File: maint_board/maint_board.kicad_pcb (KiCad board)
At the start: 2 copper layers, 175.4 x 134.9 mm, 108 parts, among them J1 USB_mini_micro_B, J2 4P4C, J3 TC2030-IDC_FB, K1 KEYSW, K10 KEYSW, K11 KEYSW, K12 KEYSW, K13 KEYSW, K14 KEYSW, K15 KEYSW, K16 KEYSW, K17 KEYSW, K18 KEYSW, K19 KEYSW, K2 KEYSW, K20 KEYSW, K21 KEYSW, K22 KEYSW, K23 KEYSW, K24 KEYSW, K25 KEYSW, K26 KEYSW, K27 KEYSW, K28 KEYSW, K29 KEYSW, K3 KEYSW, K30 KEYSW, K31 KEYSW, K32 KEYSW, K4 KEYSW, K5 KEYSW, K6 KEYSW, K7 KEYSW, K8 KEYSW, K9 KEYSW, SW1 SW_PUSH, U1 ATMEGA32U4, X1 XTAL_GND

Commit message: added libs and worked on layout
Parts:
- removed D14, D21, D22, D23, D24, D25, D26, D27, D28, D32, D7: D, keyboard_parts:D_SOD123_axial
- removed K14, K21, K22, K23, K24, K25, K26, K27, K28, K32, K7: KEYSW, keyswitches:SW_MX_reversible
- moved D31 47.3 mm to (185.7, 97.0)
- moved K31 47.3 mm to (186.2, 92.8)
- moved D30 35.3 mm to (168.6, 114.4)
- moved K30 35.3 mm to (169.5, 110.3)
- moved D29 34.3 mm to (152.5, 111.2)
- moved K29 34.3 mm to (153.1, 107.2)
- moved C13 24.5 mm to (120.5, 105.4)
- moved C15 24.5 mm to (112.4, 105.4)
- moved C10 24.5 mm to (136.5, 105.4)
- moved C11 24.5 mm to (128.5, 105.4)
- moved C12 24.5 mm to (128.5, 105.4)
- moved C14 24.5 mm to (120.5, 105.4)
- moved C16 24.5 mm to (112.4, 105.4)
- moved C9 24.5 mm to (136.5, 105.4)
- moved D33 24.5 mm to (136.5, 101.4)
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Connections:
- D29 pad 1: /keys/Row5 -> /keys/Row4
- D30 pad 1: /keys/Row5 -> /keys/Row4
- D31 pad 1: /keys/Row5 -> /keys/Row4
- U1 pad 36: /keys/Col7 -> (no net)
- U1 pad 37: /keys/Row5 -> (no net)
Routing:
- net /keys/Row4: track 238.1 -> 82.6 mm, vias 4 -> 1
- net /keys/Row5: track 138.1 -> 0.00 mm, vias 1 -> 0
- net VCC: track 209.5 -> 75.8 mm, vias 7 -> 5
- net /keys/Col7: track 108.1 -> 0.00 mm, vias 2 -> 0
- net /Leds/Din: track 7.68 -> 111.1 mm
- net /keys/Col6: track 206.1 -> 117.1 mm, vias 3 -> 1
- net /keys/Col5: track 235.3 -> 156.5 mm
- net /keys/Col4: track 240.2 -> 185.4 mm
- net /keys/Col2: track 227.0 -> 178.8 mm
- net /keys/Row3: track 217.0 -> 168.9 mm, vias 5 -> 2
- net /keys/Col3: track 204.4 -> 156.8 mm
- net /keys/Row2: track 207.5 -> 174.2 mm, vias 5 -> 4
- net /keys/Col1: track 261.3 -> 234.8 mm
- net GND: track 101.3 -> 80.8 mm, vias 24 -> 18
- net /keys/Row1: track 197.8 -> 182.4 mm, vias 2 -> 3
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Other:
- board outline removed

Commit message: Finiched!
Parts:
- added D7: LED, Diode_SMD:D_0603_1608Metric, F.Cu at (170.3, 31.1)
- added Q1: Q_NMOS_GSD, Package_TO_SOT_SMD:SOT-23, F.Cu at (166.9, 32.0)
- added R10: 10k, Resistor_SMD:R_0603_1608Metric, F.Cu at (163.5, 33.0)
- added R9: 500, Resistor_SMD:R_0603_1608Metric, F.Cu at (173.4, 31.1)
- J1: footprint keyboard_parts:USB_miniB_hirose_5S8 -> my_connectors:usb_minib_wm5462ct-nd
- J3: footprint my_connectors:TC2030-IDC-FP -> Connector:Tag-Connect_TC2030-IDC-NL_2x03_P1.27mm_Vertical
- R1, SW1: moved to F.Cu
- moved SW1 30.0 mm to (162.4, 36.9), turned to 0 degrees
- moved R1 28.5 mm to (166.5, 36.9), turned to 180 degrees
- moved D44 21.5 mm to (181.4, 38.4)
- moved D43 19.0 mm to (178.5, 38.4)
- moved C5 18.6 mm to (200.9, 62.8), turned to 270 degrees
- moved C7 17.9 mm to (187.8, 57.2), turned to 180 degrees
- moved J1 17.3 mm to (180.6, 30.6), turned to 270 degrees
- moved D30 14.0 mm to (182.6, 113.7), turned to 350 degrees
- moved K30 13.7 mm to (183.2, 108.9)
- moved D29 12.6 mm to (165.1, 110.4), turned to 350 degrees
- moved K29 12.5 mm to (165.6, 105.9)
- moved J3 5.58 mm to (181.0, 52.0), turned to 90 degrees
- moved R4 5.43 mm to (192.7, 45.7)
- moved R5 4.84 mm to (197.8, 45.6)
- moved J2 3.83 mm to (196.1, 35.0)
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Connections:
- U1 pad 37: (no net) -> Net-(Q1-Pad1)
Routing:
- net VCC: track 75.8 -> 279.0 mm, vias 5 -> 22
- net Net-(Q1-Pad1): track 0.00 -> 64.2 mm, vias 0 -> 3
- net Net-(R1-Pad2): track 0.00 -> 42.2 mm, vias 0 -> 1
- net /mcu/usb_D-: track 5.20 -> 36.7 mm
- net /mcu/usb_D+: track 5.80 -> 34.5 mm
- net GND: track 80.8 -> 106.6 mm, vias 18 -> 30
- net /keys/Col1: track 234.8 -> 210.2 mm, vias 2 -> 1
- net rst_prog: track 0.00 -> 18.9 mm
- net sck_prog: track 0.00 -> 17.3 mm
- net /keys/Col5: track 156.5 -> 172.6 mm, vias 2 -> 3
- net /keys/Col4: track 185.4 -> 201.0 mm
- net mosi_prog: track 0.00 -> 14.4 mm
- net miso_prog: track 0.00 -> 14.0 mm
- net /keys/Row2: track 174.2 -> 160.9 mm, vias 4 -> 0
- net /mcu/SCL: track 29.5 -> 42.6 mm, vias 2 -> 3
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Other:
- board outline added: 151.1 x 90.3 mm
- net class Default: clearance 0.3 -> 0.25
- net class Min added: clearance 0.1, trace_width 0.1, via_dia 0.45, via_drill 0.2
- rule pad_to_mask_clearance: 0.051 -> 0
- rule solder_mask_min_width: 0.25 -> 0.1
- rule trace_clearance: 0.3 -> 0.25
- rule trace_min: 0.2 -> 0.1
- rule via_min_drill: 0.3 -> 0.2
- rule via_min_size: 0.4 -> 0.45

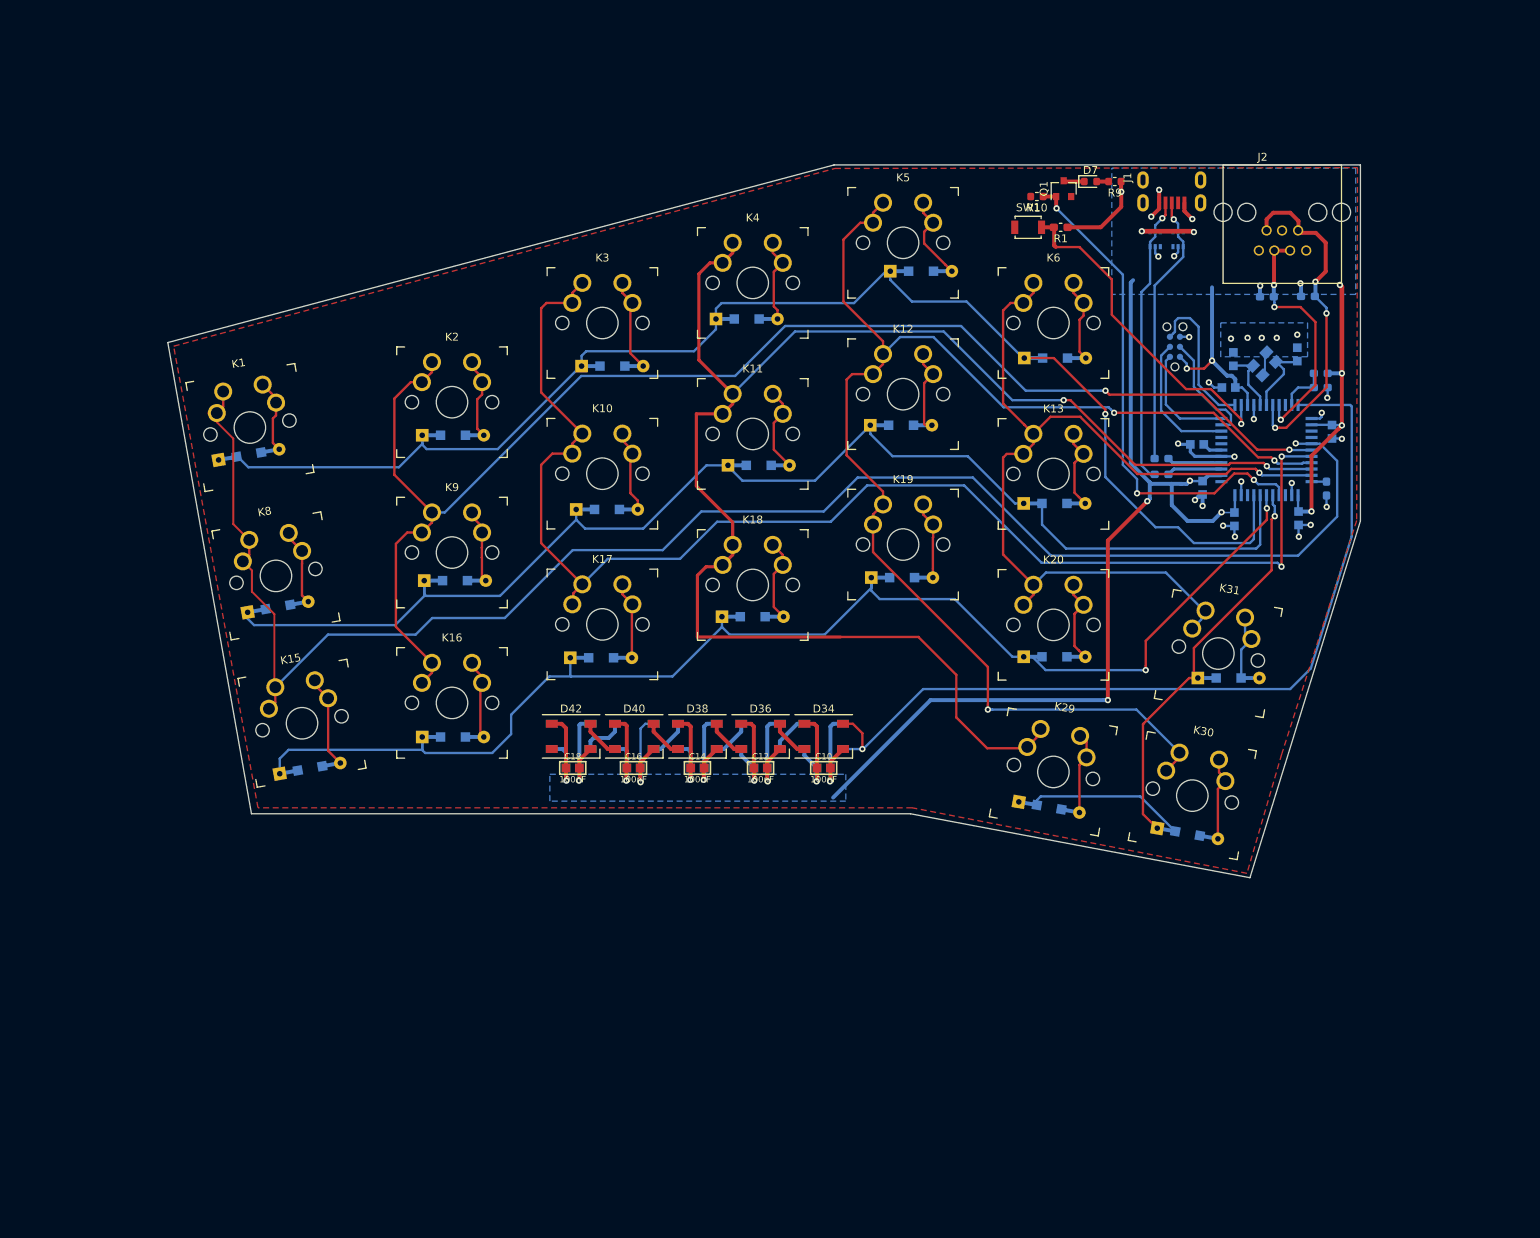
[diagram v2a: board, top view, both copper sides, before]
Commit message: Added mounting holes
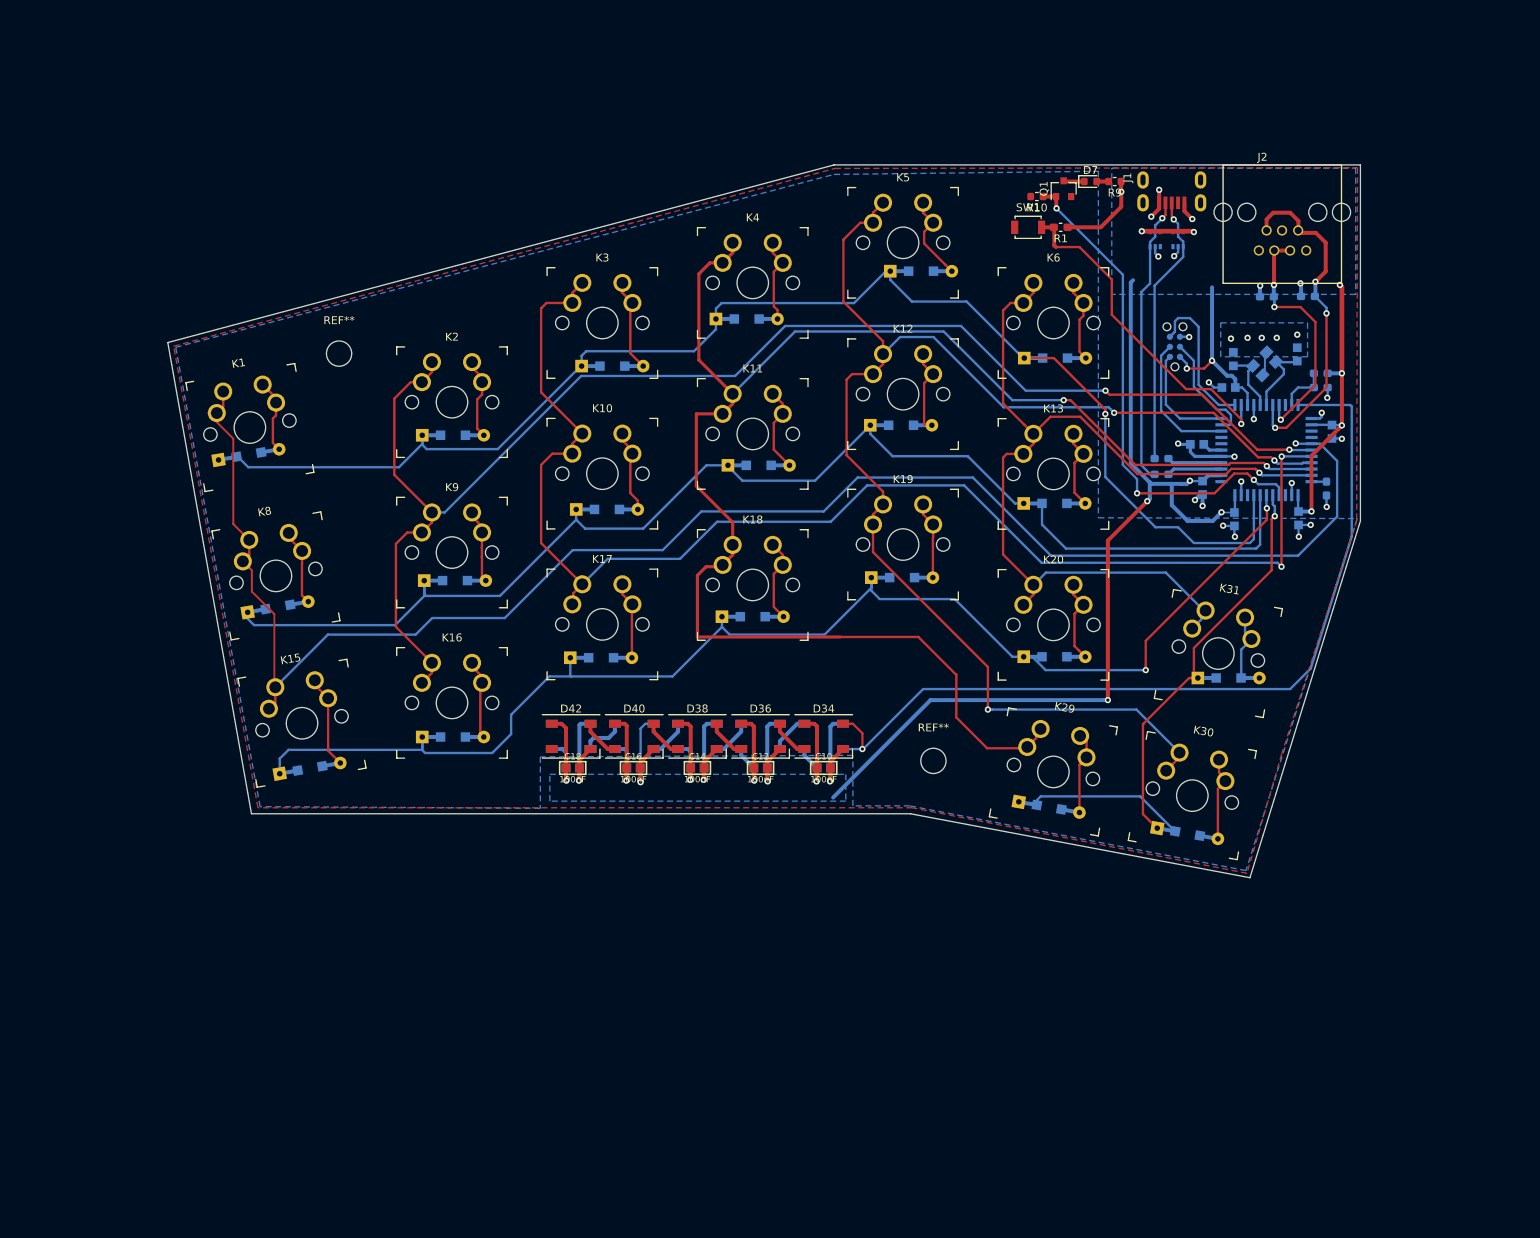
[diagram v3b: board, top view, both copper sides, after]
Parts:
- added REF**: MountingHole_3.2mm_M3, MountingHole:MountingHole_3.2mm_M3, F.Cu at (150.4, 104.5)
- added REF**: MountingHole_3.2mm_M3, MountingHole:MountingHole_3.2mm_M3, F.Cu at (75.1, 52.9)
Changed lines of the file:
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@@
     (tracks 931)
     (zones 0)
-    (modules 90)
+    (modules 92)
     (nets 62)
   )
   (page A4)
   (layers
-    (0 F.Cu signal hide)
-    (31 B.Cu signal)
+    (0 F.Cu signal)
+    (31 B.Cu signal hide)
     (32 B.Adhes user)
     (33 F.Adhes user)
@@
   )
   (setup
-    (last_trace_width 0.3)
+    (last_trace_width 0.25)
     (user_trace_width 0.1)
     (user_trace_width 0.2)
@@
     (diff_pair_gap 0.12)
   )
+  (module MountingHole:MountingHole_3.2mm_M3 (layer F.Cu)
+    (at 150.4 104.5)
+    (descr "Mounting Hole 3.2mm, no annular, M3")
+    (tags "mounting hole 3.2mm no annular m3")
+    (solder_mask_margin 2)
+    (clearance 2)
+    (attr virtual)
+    (fp_text reference REF** (at 0 -4.2) (layer F.SilkS)
+      (effects (font (size 1 1) (thickness 0.15)))
+    )
+    (fp_text value MountingHole_3.2mm_M3 (at 0 4.2) (layer F.Fab)
+      (effects (font (size 1 1) (thickness 0.15)))
+    )
+    (fp_text user %R (at 0.3 0) (layer F.Fab)
+      (effects (font (size 1 1) (thickness 0.15)))
+    )
+    (fp_circle (center 0 0) (end 3.2 0) (layer Cmts.User) (width 0.15))
+    (fp_circle (center 0 0) (end 3.45 0) (layer F.CrtYd) (width 0.05))
+    (pad 1 np_thru_hole circle (at 0 0) (size 3.2 3.2) (drill 3.2) (layers *.Cu *.Mask))
+  )
+  (module MountingHole:MountingHole_3.2mm_M3 (layer F.Cu)
+    (at 75.1 52.9)
+    (descr "Mounting Hole 3.2mm, no annular, M3")
+    (tags "mounting hole 3.2mm no annular m3")
+    (solder_mask_margin 2)
+    (clearance 2)
+    (attr virtual)
+    (fp_text reference REF** (at 0 -4.2) (layer F.SilkS)
+      (effects (font (size 1 1) (thickness 0.15)))
+    )
+    (fp_text value MountingHole_3.2mm_M3 (at 0 4.2) (layer F.Fab)
+      (effects (font (size 1 1) (thickness 0.15)))
+    )
+    (fp_circle (center 0 0) (end 3.45 0) (layer F.CrtYd) (width 0.05))
+    (fp_circle (center 0 0) (end 3.2 0) (layer Cmts.User) (width 0.15))
+    (fp_text user %R (at 0.3 0) (layer F.Fab)
+      (effects (font (size 1 1) (thickness 0.15)))
+    )
+    (pad 1 np_thru_hole circle (at 0 0) (size 3.2 3.2) (drill 3.2) (layers *.Cu *.Mask))
+  )
   (module keyboard_parts:D_SOD123_axial (layer B.Cu)
     (at 187.8 94)
@@
     (pad "" thru_hole oval (at 0.3 -3.65 270) (size 2.2 1.45) (drill oval 1.4 0.65) (layers *.Cu *.Mask))
     (pad "" thru_hole oval (at 3.2 3.65 270) (size 2.2 1.45) (drill oval 1.4 0.65) (layers *.Cu *.Mask))
+    (model /home/torbjorn/development/kicad/my_3d_moduels/513870578.stp
+      (offset (xyz -3 0 2.5))
+      (scale (xyz 1 1 1))
+      (rotate (xyz -90 0 90))
+    )
   )
   (module Resistor_SMD:R_0603_1608Metric_Pad1.05x0.95mm_HandSolder (layer F.Cu)
@@
   )
   (zone (net 1) (net_name GND) (layer B.Cu) (hatch edge 0.508)
-    (priority 1)
+    (priority 3)
     (connect_pads (clearance 0.508))
     (min_thickness 0.254)
@@
       )
     )
+  )
+  (zone (net 1) (net_name GND) (layer B.Cu) (hatch edge 0.508)
+    (priority 2)
+    (connect_pads (clearance 0.508))
+    (min_thickness 0.254)
+    (fill yes (arc_segments 32) (thermal_gap 0.508) (thermal_bridge_width 0.508))
+    (polygon
+      (pts
+        (xy 171.3 73.7) (xy 204.1 73.8) (xy 190 118.4) (xy 147.4 110.2) (xy 140.2 110.2)
+        (xy 140.2 103.8) (xy 100.6 104) (xy 100.6 110.5) (xy 65.1 110.3) (xy 54.4 52.1)
+        (xy 137.8 30.2) (xy 171.3 29.8)
+      )
+    )

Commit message: Added silc art and rounded corners
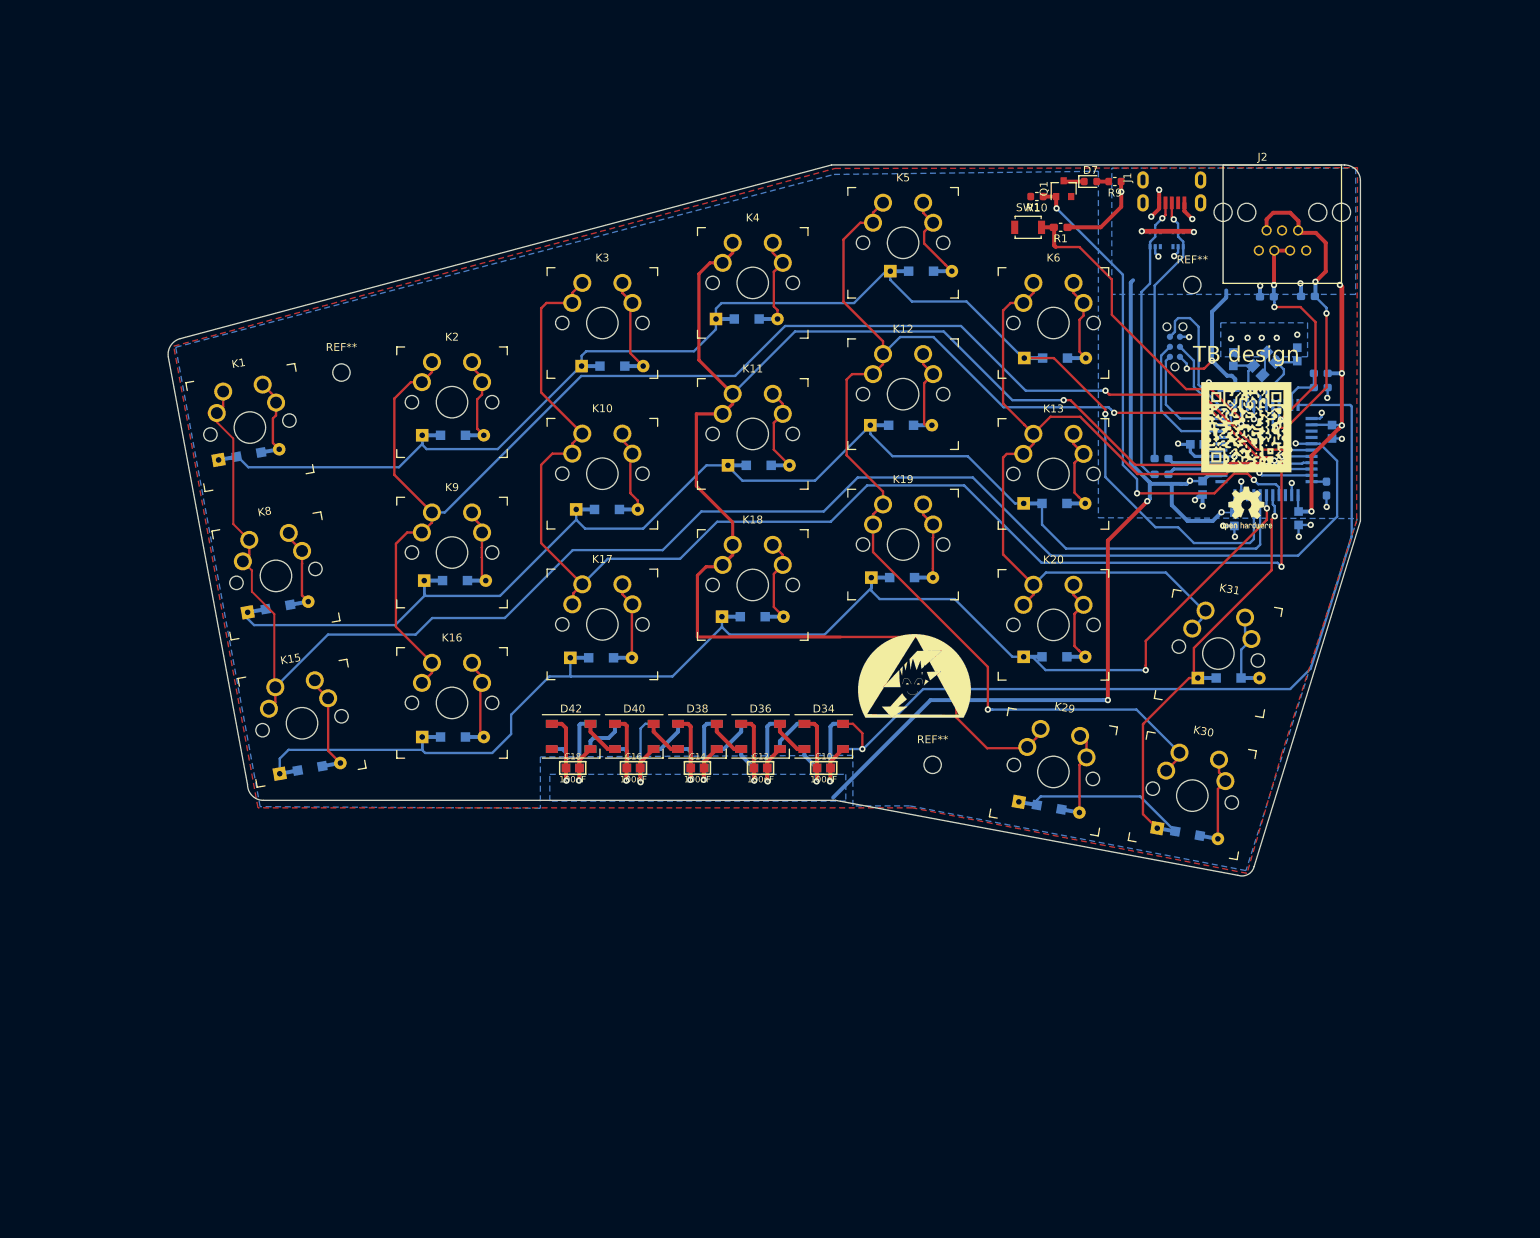
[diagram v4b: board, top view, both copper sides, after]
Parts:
- removed the REF** at (150.4, 104.5)
- removed the REF** at (75.1, 52.9)
- added G***: LOGO, grafic:loggo2, F.Cu at (148.0, 95.5)
- added G***: LOGO, grafic:qr, F.Cu at (190.0, 62.2)
- added REF**: OSHW-Logo2_7.3x6mm_SilkScreen, Symbol:OSHW-Logo2_7.3x6mm_SilkScreen, F.Cu at (190.0, 72.5)
- added REF**: MountingHole_2.2mm_M2, MountingHole:MountingHole_2.2mm_M2, F.Cu at (183.2, 44.2)
- added REF**: MountingHole_2.2mm_M2, MountingHole:MountingHole_2.2mm_M2, F.Cu at (150.3, 105.0)
- added REF**: MountingHole_2.2mm_M2, MountingHole:MountingHole_2.2mm_M2, F.Cu at (75.4, 55.3)
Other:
- board size 151.1 x 90.3 mm -> 151.1 x 90.1 mm
- board text added: "TB design"
